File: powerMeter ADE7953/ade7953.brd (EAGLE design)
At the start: 46.3 x 43.5 mm, 44 parts, among them IC1 ADE7953

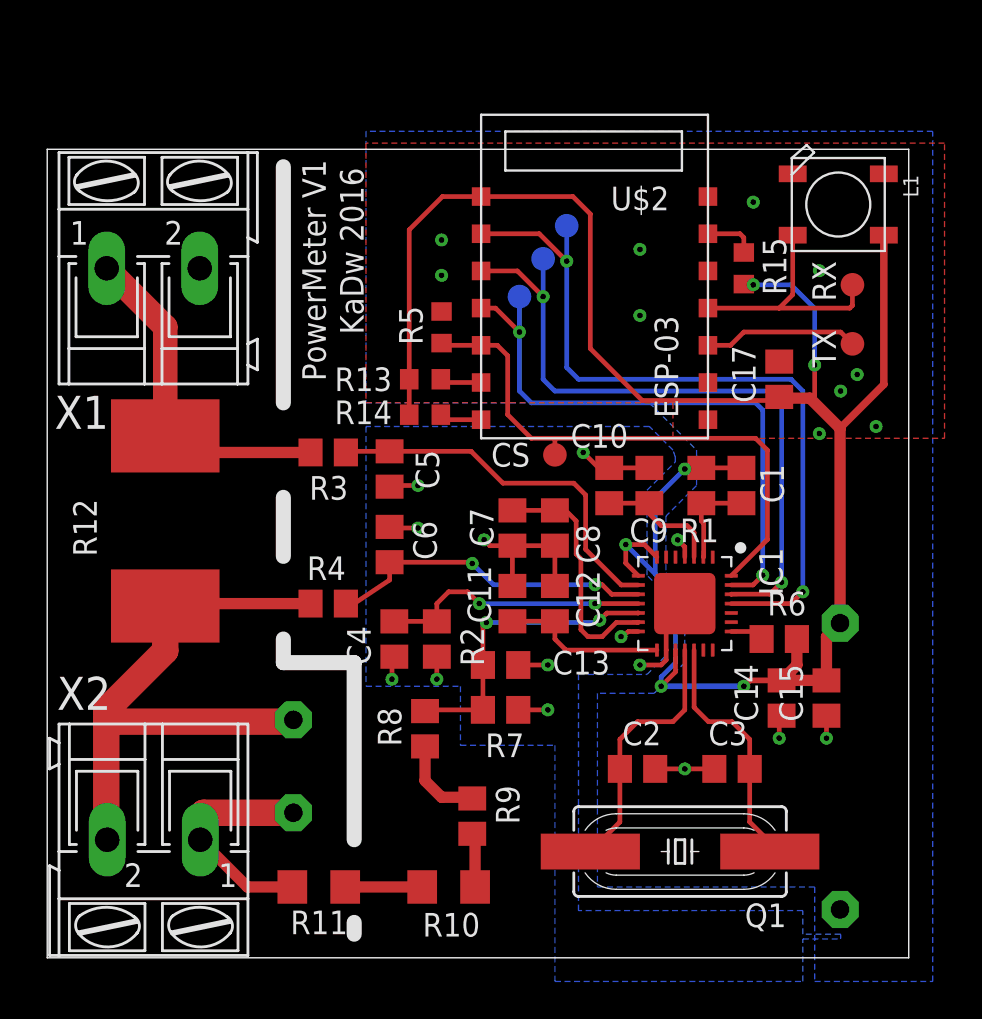
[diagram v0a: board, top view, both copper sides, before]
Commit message: updated WiSwitch, tiny433mhz and ade7953
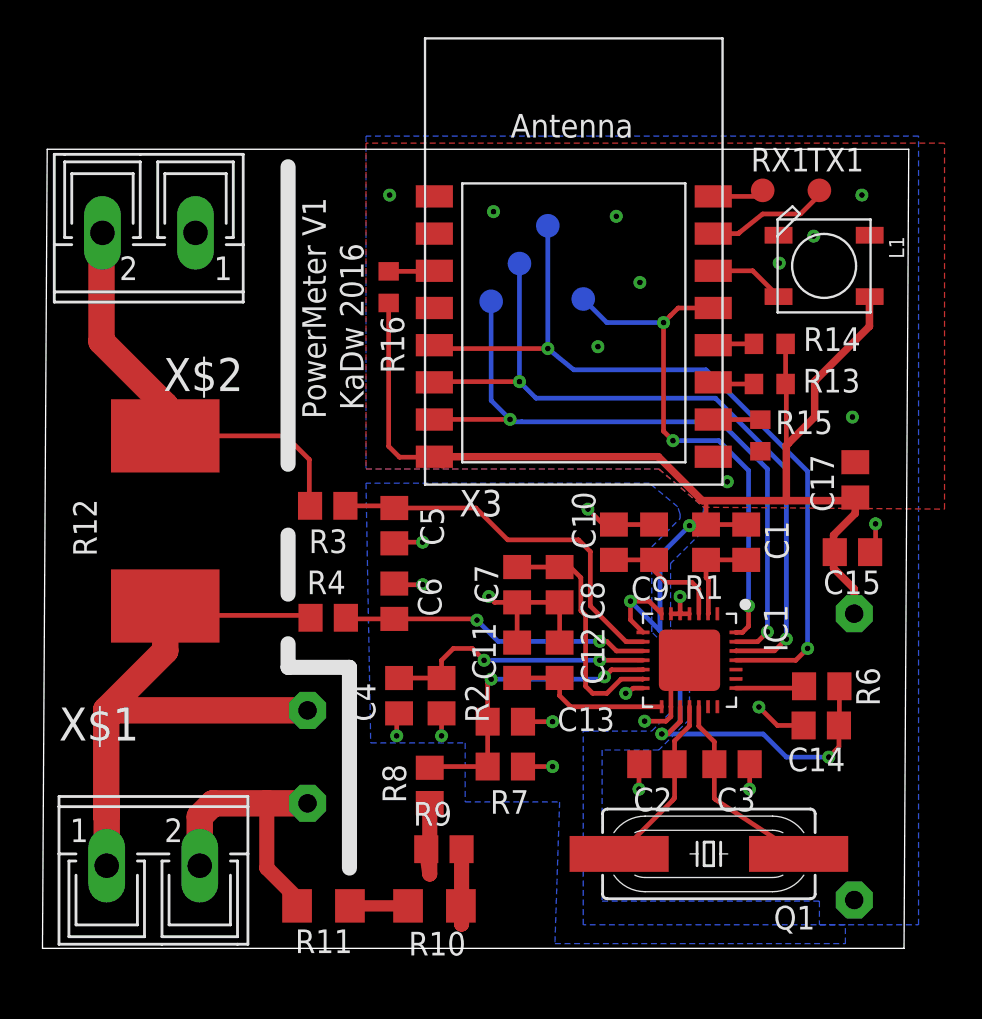
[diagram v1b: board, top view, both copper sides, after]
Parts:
- removed R5: (no value), rcl:R0603
- removed RX, TX: PTR1B1,27, testpad:B1,27
- removed U$2: ESP8266_ESP-03, ESP8266:ESP-03
- removed X1, X2: (no value), con-ptr500:AK300/2
- added R16: (no value), rcl:R0603
- added RX1, TX1: PTR1B1,27, testpad:B1,27
- added X$1, X$2: ARK2, _ARK:ARK2
- added X3: (no value), adafruit:ESP-12
- moved R14 18.9 mm to (35.7, 89.5), turned to 0 degrees
- moved R13 18.5 mm to (35.7, 87.4), turned to 0 degrees
- moved R15 9.04 mm to (35.2, 84.6), turned to 90 degrees
- moved CS 8.52 mm to (25.7, 91.9), flipped to the bottom
- moved C15 7.97 mm to (40.1, 78.3), turned to 180 degrees
- moved C17 6.78 mm to (40.3, 82.2)
- moved R6 3.42 mm to (38.5, 71.1)
- moved L1 3.39 mm to (38.6, 93.7)
- moved C1 3.06 mm to (34.4, 78.9)
- moved R1 3.06 mm to (32.3, 78.9)
- moved C10 3.06 mm to (27.3, 78.9)
- moved C11 3.06 mm to (22.1, 72.5)
- moved C12 3.06 mm to (24.4, 72.5)
- moved C13 3.06 mm to (21.5, 69.2)
- moved C4 3.06 mm to (15.7, 70.6)
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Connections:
- removed net N$3: R15.1, U$2.6
- removed net RX1: L1.4-DIN, RX.TP, U$2.4
- removed net TX1: TX.TP, U$2.3
- new net GPIO15: R15.2, X3.10
- new net GPIO4: L1.4-DIN, X3.14
- new net N$4: R16.1, X3.3
- new net RX: TX1.TP, X3.15
- new net TX: RX1.TP, X3.16
- net CS: now also X3.13; no longer R5.2, U$2.12
- net GND: now also IC1.5, IC1.6, R15.1, X3.9; no longer R5.1, U$2.1
- net GPIO0: now also X3.12; no longer U$2.14
- net GPIO2: now also X3.11; no longer U$2.13
- net HOT: now also X$1.2; no longer X2.1
- net MISO: now also X3.6; no longer U$2.10
- net MOSI: now also X3.7; no longer U$2.11
- net SCLK: now also X3.5; no longer U$2.9
- net SHUNT_HIGH: now also X$2.2; no longer X1.1
- net SHUNT_LOW: now also X$1.1; no longer X2.2
- net VCC: now also R16.2, X3.8; no longer R15.2, U$2.8
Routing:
- net VCC: track 115.6 -> 99.6 mm, vias 6 -> 4
- net RX1: track 13.2 -> 0.00 mm
- net TX1: track 8.33 -> 0.00 mm
- net RX: track 0.00 -> 6.76 mm
- net SHUNT_HIGH: track 18.5 -> 24.4 mm
- net CLKIN: track 14.1 -> 9.48 mm
- net MOSI: track 32.0 -> 36.5 mm
- net GPIO4: track 0.00 -> 4.09 mm
- net CLKOUT: track 14.7 -> 10.7 mm
- net SHUNT_LOW: track 32.6 -> 36.1 mm
- net MISO: track 36.3 -> 39.4 mm
- net N$3: track 2.81 -> 0.00 mm
- net TX: track 0.00 -> 2.80 mm
- net HOT: track 12.3 -> 14.9 mm
- net GPIO15: track 0.00 -> 2.54 mm
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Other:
- board size 46.3 x 43.5 mm -> 46.6 x 43 mm
